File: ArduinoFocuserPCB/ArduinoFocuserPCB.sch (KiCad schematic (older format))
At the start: 12 parts, among them M1 Stepper_Motor_bipolar, SW1 Rotary_Encoder_Switch, U1 DHT11

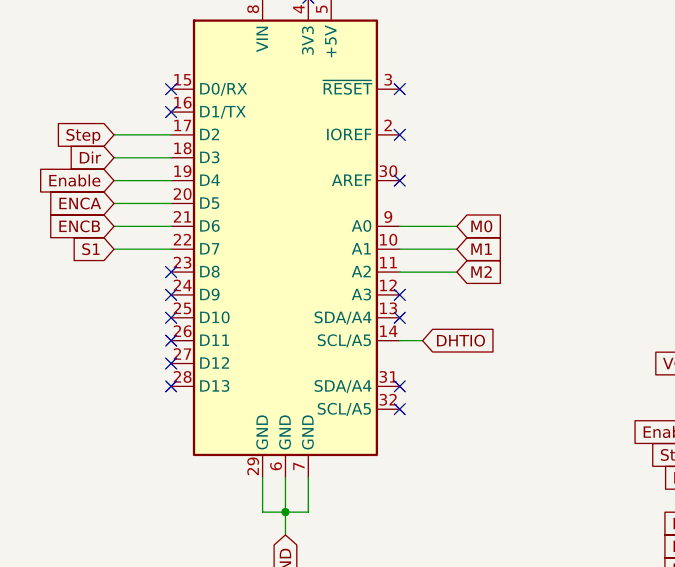
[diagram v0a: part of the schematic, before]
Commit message: created traces
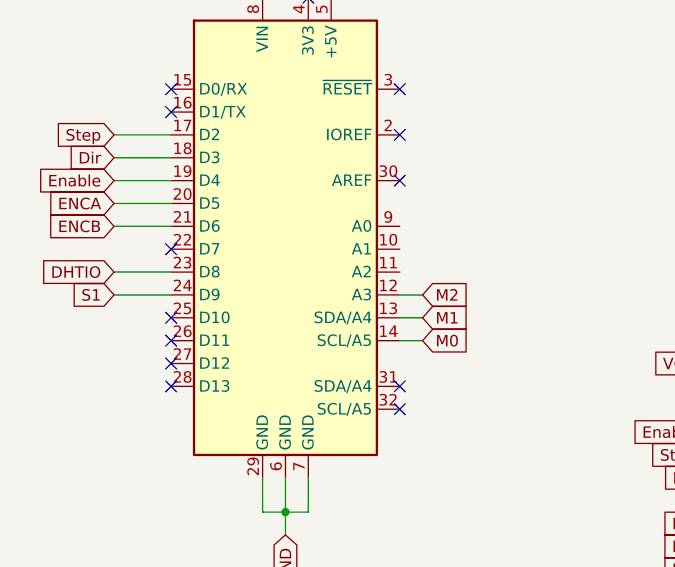
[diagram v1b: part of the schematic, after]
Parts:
- C1, C2, C3: footprint (none) -> Capacitor_THT:C_Disc_D3.0mm_W2.0mm_P2.50mm
- M1: footprint (none) -> TerminalBlock:TerminalBlock_bornier-4_P5.08mm
- R1, R2, R3, R4: footprint (none) -> Resistor_THT:R_Axial_DIN0204_L3.6mm_D1.6mm_P5.08mm_Horizontal
- SW1: footprint (none) -> Rotary_Encoder:RotaryEncoder_Alps_EC11E-Switch_Vertical_H20mm
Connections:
- net DHTIO: now also A1.23 (D8); no longer A1.14 (SCL/A5)
- net M0: now also A1.14 (SCL/A5); no longer A1.9 (A0)
- net M1: now also A1.13 (SDA/A4); no longer A1.10 (A1)
- net M2: now also A1.12 (A3); no longer A1.11 (A2)
- net S1: now also A1.24 (D9); no longer A1.22 (D7)
- no-connect marks 17 -> 14
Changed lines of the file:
@@
 $EndDescr
-$Comp
-L MCU_Module:Arduino_UNO_R3 A1
-U 1 1 5E42D953
-P 2100 3400
-F 0 "A1" H 2100 4581 50  0000 C CNN
-F 1 "Arduino_UNO_R3" H 2100 4490 50  0000 C CNN
-F 2 "Module:Arduino_UNO_R3" H 2100 3400 50  0001 C CIN
-F 3 "https://www.arduino.cc/en/Main/arduinoBoardUno" H 2100 3400 50  0001 C CNN
-	1    2100 3400
-	1    0    0    -1
-$EndComp
 $Comp
 L Driver_Motor:Pololu_Breakout_DRV8825 DRV1
@@
 F 0 "M1" V 5868 4012 50  0000 R CNN
 F 1 "Stepper_Motor_bipolar" V 5777 4012 50  0000 R CNN
-F 2 "" H 5910 4190 50  0001 C CNN
+F 2 "TerminalBlock:TerminalBlock_bornier-4_P5.08mm" H 5910 4190 50  0001 C CNN
 F 3 "http://www.infineon.com/dgdl/Application-Note-TLE8110EE_driving_UniPolarStepperMotor_V1.1.pdf?fileId=db3a30431be39b97011be5d0aa0a00b0" H 5910 4190 50  0001 C CNN
 	1    5900 4200
@@
 F 0 "SW1" V 8846 1370 50  0000 R CNN
 F 1 "Rotary_Encoder_Switch" V 8755 1370 50  0000 R CNN
-F 2 "" H 8650 1760 50  0001 C CNN
+F 2 "Rotary_Encoder:RotaryEncoder_Alps_EC11E-Switch_Vertical_H20mm" H 8650 1760 50  0001 C CNN
 F 3 "~" H 8800 1860 50  0001 C CNN
 	1    8800 1600
@@
 F 0 "R3" V 9207 2350 50  0000 C CNN
 F 1 "10k" V 9116 2350 50  0000 C CNN
-F 2 "" V 8930 2350 50  0001 C CNN
+F 2 "Resistor_THT:R_Axial_DIN0204_L3.6mm_D1.6mm_P5.08mm_Horizontal" V 8930 2350 50  0001 C CNN
 F 3 "~" H 9000 2350 50  0001 C CNN
 	1    9000 2350
@@
 F 0 "C3" H 9615 2196 50  0000 L CNN
 F 1 ".01uF" H 9615 2105 50  0000 L CNN
-F 2 "" H 9538 2000 50  0001 C CNN
+F 2 "Capacitor_THT:C_Disc_D3.0mm_W2.0mm_P2.50mm" H 9538 2000 50  0001 C CNN
 F 3 "~" H 9500 2150 50  0001 C CNN
 	1    9500 2150
@@
 F 0 "C2" H 7900 2150 50  0000 L CNN
 F 1 ".01uF" H 7800 2050 50  0000 L CNN
-F 2 "" H 8138 1950 50  0001 C CNN
+F 2 "Capacitor_THT:C_Disc_D3.0mm_W2.0mm_P2.50mm" H 8138 1950 50  0001 C CNN
 F 3 "~" H 8100 2100 50  0001 C CNN
 	1    8100 2100
@@
 F 0 "R2" V 8393 2350 50  0000 C CNN
 F 1 "10k" V 8484 2350 50  0000 C CNN
-F 2 "" V 8530 2350 50  0001 C CNN
+F 2 "Resistor_THT:R_Axial_DIN0204_L3.6mm_D1.6mm_P5.08mm_Horizontal" V 8530 2350 50  0001 C CNN
 F 3 "~" H 8600 2350 50  0001 C CNN
 	1    8600 2350
@@
 F 0 "R1" H 8400 2300 50  0000 R CNN
 F 1 "10k" H 8450 2400 50  0000 R CNN
-F 2 "" V 8180 2350 50  0001 C CNN
+F 2 "Resistor_THT:R_Axial_DIN0204_L3.6mm_D1.6mm_P5.08mm_Horizontal" V 8180 2350 50  0001 C CNN
 F 3 "~" H 8250 2350 50  0001 C CNN
 	1    8250 2350
@@
 F 0 "R4" V 9143 2350 50  0000 C CNN
 F 1 "10k" V 9234 2350 50  0000 C CNN
-F 2 "" V 9280 2350 50  0001 C CNN
+F 2 "Resistor_THT:R_Axial_DIN0204_L3.6mm_D1.6mm_P5.08mm_Horizontal" V 9280 2350 50  0001 C CNN
 F 3 "~" H 9350 2350 50  0001 C CNN
 	1    9350 2350
@@
 F 0 "C1" H 5215 3546 50  0000 L CNN
 F 1 ".01uF" H 5215 3455 50  0000 L CNN
-F 2 "" H 5138 3350 50  0001 C CNN
+F 2 "Capacitor_THT:C_Disc_D3.0mm_W2.0mm_P2.50mm" H 5138 3350 50  0001 C CNN
 F 3 "~" H 5100 3500 50  0001 C CNN
 	1    5100 3500
@@
 Wire Wire Line
 	2200 4650 2100 4650
-Text GLabel 2700 3900 2    50   Input ~ 0
+Text GLabel 1350 3600 0    50   Input ~ 0
 DHTIO
 Wire Wire Line
@@
 Wire Wire Line
 	1350 3400 1600 3400
-Text GLabel 2850 3400 2    50   Input ~ 0
+Text GLabel 2700 3900 2    50   Input ~ 0
 M0
-Text GLabel 2850 3500 2    50   Input ~ 0
+Text GLabel 2700 3800 2    50   Input ~ 0
 M1
-Text GLabel 2850 3600 2    50   Input ~ 0
+Text GLabel 2700 3700 2    50   Input ~ 0
 M2
-Wire Wire Line
-	2600 3400 2850 3400
-Wire Wire Line
-	2600 3500 2850 3500
-Wire Wire Line
-	2600 3600 2850 3600
 $Comp
 L power:GND #PWR0101
@@
 NoConn ~ 2600 3000
 NoConn ~ 2600 3200
-NoConn ~ 2600 3700
-NoConn ~ 2600 3800
 NoConn ~ 2600 4100
 NoConn ~ 2600 4200
-NoConn ~ 1600 3600
-NoConn ~ 1600 3700
 NoConn ~ 1600 3800
 NoConn ~ 1600 3900
@@
 Wire Wire Line
 	8900 1200 8900 1300
-Text GLabel 1350 3500 0    50   Input ~ 0
-S1
-Wire Wire Line
-	1350 3500 1600 3500
 NoConn ~ 1600 4100
 NoConn ~ 4250 3900
 NoConn ~ 1600 2800
 NoConn ~ 1600 2900
+Wire Wire Line
+	2600 3700 2700 3700
+Wire Wire Line
+	2600 3800 2700 3800
+$Comp
+L MCU_Module:Arduino_UNO_R3 A1
+U 1 1 5E42D953
+P 2100 3400
+F 0 "A1" H 2100 4581 50  0000 C CNN
+F 1 "Arduino_UNO_R3" H 2100 4490 50  0000 C CNN
+F 2 "Module:Arduino_UNO_R3" H 2100 3400 50  0001 C CIN
+F 3 "https://www.arduino.cc/en/Main/arduinoBoardUno" H 2100 3400 50  0001 C CNN
+	1    2100 3400
+	1    0    0    -1
+$EndComp
+Wire Wire Line
+	1350 3600 1600 3600
+Text GLabel 1350 3700 0    50   Input ~ 0
+S1
+Wire Wire Line
+	1350 3700 1600 3700
+NoConn ~ 1600 3500
 $EndSCHEMATC

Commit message: trigger added. some routing. needed restart checkpoint
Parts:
- added U2: SN74HC14N, digikey-footprints:DIP-14_W3mm, symbol dk_Logic-Gates-and-Inverters:SN74HC14N
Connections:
- net +5V: now also U2.14 (VCC)
- net DHTIO: now also A1.28 (D13); no longer A1.23 (D8)
- net ENCA: now also U2.5 (3A); no longer A1.20 (D5)
- net ENCB: now also U2.3 (2A); no longer A1.21 (D6)
- net GND: now also U2.7 (GND)
- net S1: now also U2.1 (1A); no longer A1.24 (D9)
- new net ENCA_A: A1.20 (D5)
- new net ENCB_A: A1.21 (D6), U2.4 (2Y), U2.6 (3Y)
- new net S1_A: A1.24 (D9), U2.2 (1Y)
- no-connect marks 14 -> 17
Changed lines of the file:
@@
 Wire Wire Line
 	2200 4650 2100 4650
-Text GLabel 1350 3600 0    50   Input ~ 0
+Text GLabel 1350 4100 0    50   Input ~ 0
 DHTIO
 Wire Wire Line
 	2600 3900 2700 3900
 Text GLabel 1350 3300 0    50   Input ~ 0
-ENCA
+ENCA_A
 Text GLabel 1350 3400 0    50   Input ~ 0
-ENCB
+ENCB_A
 Wire Wire Line
 	1350 3300 1600 3300
@@
 Wire Wire Line
 	8900 1200 8900 1300
-NoConn ~ 1600 4100
 NoConn ~ 4250 3900
 NoConn ~ 1600 2800
@@
 	1    0    0    -1
 $EndComp
-Wire Wire Line
-	1350 3600 1600 3600
 Text GLabel 1350 3700 0    50   Input ~ 0
-S1
+S1_A
 Wire Wire Line
 	1350 3700 1600 3700
 NoConn ~ 1600 3500
+$Comp
+L dk_Logic-Gates-and-Inverters:SN74HC14N U2
+U 1 1 5E47ABFB
+P 4800 1950
+F 0 "U2" H 4800 2753 60  0000 C CNN
+F 1 "SN74HC14N" H 4800 2647 60  0000 C CNN
+F 2 "digikey-footprints:DIP-14_W3mm" H 5000 2150 60  0001 L CNN
+F 3 "http://www.ti.com/general/docs/suppproductinfo.tsp?distId=10&gotoUrl=http%3A%2F%2Fwww.ti.com%2Flit%2Fgpn%2Fsn74hc14" H 5000 2250 60  0001 L CNN
+F 4 "296-1577-5-ND" H 5000 2350 60  0001 L CNN "Digi-Key_PN"
+F 5 "SN74HC14N" H 5000 2450 60  0001 L CNN "MPN"
+F 6 "Integrated Circuits (ICs)" H 5000 2550 60  0001 L CNN "Category"
+F 7 "Logic - Gates and Inverters" H 5000 2650 60  0001 L CNN "Family"
+F 8 "http://www.ti.com/general/docs/suppproductinfo.tsp?distId=10&gotoUrl=http%3A%2F%2Fwww.ti.com%2Flit%2Fgpn%2Fsn74hc14" H 5000 2750 60  0001 L CNN "DK_Datasheet_Link"
+F 9 "/product-detail/en/texas-instruments/SN74HC14N/296-1577-5-ND/277223" H 5000 2850 60  0001 L CNN "DK_Detail_Page"
+F 10 "IC INVERTER SCHMITT 6CH 14DIP" H 5000 2950 60  0001 L CNN "Description"
+F 11 "Texas Instruments" H 5000 3050 60  0001 L CNN "Manufacturer"
+F 12 "Active" H 5000 3150 60  0001 L CNN "Status"
+	1    4800 1950
+	1    0    0    -1
+$EndComp
+Text GLabel 4350 1650 0    50   Input ~ 0
+S1
+Text GLabel 4350 1850 0    50   Input ~ 0
+ENCA
+Text GLabel 4350 1750 0    50   Input ~ 0
+ENCB
+Text GLabel 5250 1650 2    50   Input ~ 0
+S1_A
+Text GLabel 5250 1750 2    50   Input ~ 0
+ENCB_A
+Text GLabel 5250 1850 2    50   Input ~ 0
+ENCB_A
+Wire Wire Line
+	5100 1650 5250 1650
+Wire Wire Line
+	5100 1750 5250 1750
+Wire Wire Line
+	5100 1850 5250 1850
+Wire Wire Line
+	4350 1650 4500 1650
+Wire Wire Line
+	4350 1750 4500 1750
+Wire Wire Line
+	4350 1850 4500 1850
+Wire Wire Line
+	1350 4100 1600 4100
+NoConn ~ 1600 3600
+NoConn ~ 2600 3400
+NoConn ~ 2600 3500
+NoConn ~ 2600 3600
+Text GLabel 4750 1300 0    50   Input ~ 0
+VCC
+Wire Wire Line
+	4800 1350 4800 1300
+Wire Wire Line
+	4800 1300 4750 1300
+Text GLabel 4800 2500 0    50   Input ~ 0
+GND
+Wire Wire Line
+	4800 2500 4800 2450
 $EndSCHEMATC

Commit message: git ignore
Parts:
- renumbered M1 to Motor1
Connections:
- net ENCA_A: now also U2.6 (3Y)
- net ENCB_A: no longer U2.6 (3Y)
- no-connect marks 17 -> 23
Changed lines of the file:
@@
 $EndComp
 $Comp
-L Motor:Stepper_Motor_bipolar M1
+L Motor:Stepper_Motor_bipolar Motor1
 U 1 1 5E42FC2F
 P 5900 4200
-F 0 "M1" V 5868 4012 50  0000 R CNN
+F 0 "Motor1" V 5868 4012 50  0000 R CNN
 F 1 "Stepper_Motor_bipolar" V 5777 4012 50  0000 R CNN
 F 2 "TerminalBlock:TerminalBlock_bornier-4_P5.08mm" H 5910 4190 50  0001 C CNN
@@
 ENCB_A
 Text GLabel 5250 1850 2    50   Input ~ 0
-ENCB_A
+ENCA_A
 Wire Wire Line
 	5100 1650 5250 1650
@@
 Wire Wire Line
 	4800 2500 4800 2450
+NoConn ~ 5100 1950
+NoConn ~ 5100 2050
+NoConn ~ 5100 2150
+NoConn ~ 4500 2150
+NoConn ~ 4500 2050
+NoConn ~ 4500 1950
 $EndSCHEMATC
